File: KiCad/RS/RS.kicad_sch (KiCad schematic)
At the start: 81 parts, among them J1 TSM-104-01-L-SH, J2 Conn_01x04_Socket, J3 SPI1, J4 SPI2, J5 XY2500V-B(5.0)-2P, J6 Screw_Terminal_01x12, Q1 AO3400A, Q2 FMMT491A, SW1 SW_Push, U1 MCP1700T-3302E/TT, U2 LM2596S-5, U3 STM32C562KET6, U4 TLP185, U5 RV-3028-C7, Y1 24MHz CL=8pF ESR=50Ω

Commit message: ADD: ST87M01-1301 Modem.
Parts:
- removed J4: SPI2, Connector_IDC:IDC-Header_2x04_P2.54mm_Vertical_SMD, symbol Connector_Generic:Conn_02x04_Odd_Even
- removed R12, R4, R7: 10k, Resistor_SMD:R_0805_2012Metric_Pad1.20x1.40mm_HandSolder, symbol Device:R
- L2: value 1kΩ/100kHz -> 1kΩ/100MHz
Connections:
- net SPI2_MOSI is gone; now on net D_OUT1_M: U3.19 (PA8)
- net SPI2_NSS is gone; now on net RTC_CLK: U3.27 (PB4)
- net D_OUT1_M: no longer U3.20 (PA9)
- net D_OUT2_M: now also U3.20 (PA9); no longer U3.21 (PA11)
- net GND: no longer U3.31 (PB8-BOOT0)
- net I2C1_SCL: no longer R5.2, U3.29 (PB6)
- net SPI1_MISO: no longer R11.1, U3.12 (PA6)
- net SPI1_MOSI: no longer U3.28 (PB5)
- net SPI1_NSS: no longer R3.2, U3.25 (PA15)
- net SPI1_SCK: no longer U3.11 (PA5)
- net SPI2_IRQ renamed SWO
- net SPI2_MISO renamed MODEM_WAKE_UP
- net SPI2_SCK renamed MODEM_RX
- new net I2C_SCL: R5.2, U3.29 (PB6)
- new net MODEM_RST: U3.31 (PB8-BOOT0)
- new net MODEM_TX: U3.21 (PA11)
- new net SPI_MISO: R11.1, U3.12 (PA6)
- new net SPI_MOSI: U3.28 (PB5)
- new net SPI_NSS: R3.2, U3.25 (PA15)
- new net SPI_SCK: U3.11 (PA5)
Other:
- note removed: "SPI2"
- moved on the sheet: BT1, C13, C15, C17, C18, R10, R11, R13, R18, R3, R5, R6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

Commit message: FIX: BOM, SCH.
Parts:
- removed J1: TSM-104-01-L-SH, CodeDog:SAMTEC_TSM-104-01-L-SH, symbol Connector:Conn_01x04_Pin
- removed J2: Conn_01x04_Socket, CodeDog:SAMTEC_TSM-104-01-L-SH, symbol Connector:Conn_01x04_Socket
- removed J3: SPI1, Connector_IDC:IDC-Header_2x04_P2.54mm_Vertical_SMD, symbol Connector_Generic:Conn_02x04_Odd_Even
- removed Q2: FMMT491A, Package_TO_SOT_SMD:SOT-23, symbol CustomSymbols:FMMT491A
- added Q2: BC817, Package_TO_SOT_SMD:SOT-23, symbol Transistor_BJT:BC817
- added R12, R14, R15, R18, R6, R7, R8, R9: 0R, Resistor_SMD:R_0805_2012Metric_Pad1.20x1.40mm_HandSolder, symbol Device:R
- added TP5, TP6, TP7, TP8, TP9: Test Point, Connector_PinHeader_2.54mm:PinHeader_1x01_P2.54mm_Vertical, symbol Connector_Generic:Conn_01x01
- BT1: value DS1092-04-B6P -> 1056; footprint CodeDog:BatteryHolder_Keystone_106_1x20mm -> CodeDog:BAT_1056; symbol Device:Battery_Cell -> CodeDog:1056; MANUFACTURER (none) -> Keystone; MAXIMUM_PACKAGE_HEIGHT (none) -> 3.99mm; PARTREV (none) -> D; SNAPEDA_PN (none) -> 1056; STANDARD (none) -> Manufacturer Recommendations
- C1, C15, C3, C8: Mfg Part # UMK107BJ105KA-T -> GMC21X7R105K50NT; URL https://www.digikey.pl/en/products/detail/taiyo-yuden/UMK10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 -> https://www.digikey.pl/en/products/detail/cal-chip-electron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
- C11, C12: Mfg Part # 600F120JT250XT4K -> CML0805C0G120JT50V; URL https://www.digikey.pl/en/products/detail/kyocera-avx/600F1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 -> https://www.digikey.pl/en/products/detail/stackpole-electro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
- C13: Mfg Part # CC0805MRX7R0BB102 -> CL21B102KBANNNC; URL https://www.digikey.pl/en/products/detail/yageo/CC0805MRX7R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 -> https://www.digikey.pl/en/products/detail/samsung-electro-m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
- C16: Mfg Part # GRM21BR71A225KA01L -> 0805B225K250CT; URL https://www.digikey.pl/en/products/detail/murata-electronic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 -> https://www.digikey.pl/en/products/detail/walsin-technology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
- C18: value 220u/16V -> 10μ/10V; footprint Capacitor_SMD:C_1206_3216Metric -> Capacitor_SMD:C_1206_3216Metric_Pad1.33x1.80mm_HandSolder; Mfg Part # GRM31CR60J227ME11L -> GMC31Y5V106Z10NT; URL https://www.digikey.pl/en/products/detail/murata-electronic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 -> https://www.digikey.pl/en/products/detail/cal-chip-electron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
- C4: URL https://www.digikey.pl/en/products/detail/samsung-electro-m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 -> https://www.digikey.pl/en/products/detail/murata-electronic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
- D1: value B1701USD-20D000114U1930 -> LED red; URL (none) -> https://www.digikey.pl/en/products/detail/harvatek-corporat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
- D2: value B1701NG--20D000314U1930 -> LED red; Mfg Part # B1701NG--20D000314U1930 -> B1701USD-20D000114U1930; URL (none) -> https://www.digikey.pl/en/products/detail/harvatek-corporat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
- D3: symbol PCM_Diode_Schottky_AKL:SS34 -> Device:D_Schottky_Filled; URL (none) -> https://www.digikey.pl/en/products/detail/goodwork/SS56/292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
- D4: value BZV55C3V3-LGE -> 3V3; footprint Diode_SMD:D_MiniMELF -> Diode_SMD:D_SOD-523; Mfg Part # BZV55C3V3 -> BZX584B3V3; URL (none) -> https://www.digikey.pl/en/products/detail/shenzhen-slkormic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
- D5: footprint Diode_SMD:D_SOD-923 -> Diode_SMD:D_SOD-123; Mfg Part # CDZVT2R3.6B -> BZT52C3V6; URL https://www.digikey.pl/en/products/detail/rohm-semiconducto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 -> https://www.digikey.pl/en/products/detail/smc-diode-solutio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
- D6: value B1701UY--20D000214U1930 -> LED amber; URL (none) -> https://www.digikey.pl/en/products/detail/harvatek-corporat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
- J1: renamed from J5; now not fitted
- J2: renamed from J6; now not fitted
- Q1: Mfg Part # (none) -> AO3400A; URL (none) -> https://www.digikey.pl/en/products/detail/umw/AO3400A/16705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
- renumbered R8 to R10, R9 to R11, R10 to R13, R11 to R16, R13 to R17, R14 to R19, R15 to R20, R17 to R21, R19 to R22, R18 to R23, R16 to R24, R20 to R25, R21 to R26, R22 to R27, R23 to R28, R24 to R29, R25 to R30, R26 to R31, R5 to R4, R6 to R5, TP5 to TP10, TP6 to TP11, TP7 to TP12, TP8 to TP13, TP9 to TP14, TP10 to TP15, TP11 to TP16, TP12 to TP17, TP13 to TP18
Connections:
- net I2C1_SCL is gone; now on net I2C_SCL: U5.3 (SCL)
- net GND: now also BT1.N, C18.1, U3.32 (VSS), Q2.2 (E); no longer BT1.2 (-), C18.2
- net MODEM_RST: now also R7.1; no longer U3.31 (PB8-BOOT0)
- net MODEM_RX: now also R12.2; no longer U3.22 (PA12)
- net MODEM_TX: now also R14.2; no longer U3.21 (PA11)
- net MODEM_WAKE_UP: now also R15.2; no longer U3.13 (PA7)
- net at R29.2, R31.1: now also Q2.1 (B)
- net at R25.2, R26.1: now also Q2.3 (C)
- net NRST: now reaches C14.2, R10.2, SW1.2, U3.4 (NRST)
- net A_- renamed RCS
- net SPI1_IRQ renamed SPI_IRQ
- new net: R6.1, R7.2, U3.31 (PB8-BOOT0)
- new net: BT1.P, C18.2, U5.6 (VBACKUP)
- new net: R15.1, R18.2, U3.13 (PA7)
- new net: R14.1, R9.1, U3.21 (PA11)
- new net: R12.1, R8.1, U3.22 (PA12)
- new net VANT: TP9.1 (Pin_1)
- new net VEXT: TP7.1 (Pin_1)
- new net VMOD: TP6.1 (Pin_1)
- new net VMOD_PG: TP5.1 (Pin_1)
- new net VSIM: TP8.1 (Pin_1)
- new net X_MODEM_RST: R6.2
- new net X_MODEM_RX: R8.2
- new net X_MODEM_TX: R9.2
- new net X_MODEM_WAKE_UP: R18.1
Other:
- note removed: "I2C1"
- note removed: "R"
- note removed: "SPI1"
- note removed: "ST-LINK"
- note removed: "Y"
- title: Remote Sensor Module MCU Sheet -> Remote Sensor Module: PSU, MCU, Analog
- moved on the sheet: BT1, C13, C15, D4, D5, D6, Q1, R11, R13, R16, R17, R19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

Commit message: ADD: RF connections.
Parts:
- L2: footprint (none) -> Inductor_SMD:L_0805_2012Metric_Pad1.05x1.20mm_HandSolder
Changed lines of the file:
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@@
 			)
 		)
-		(property "Footprint" ""
+		(property "Footprint" "Inductor_SMD:L_0805_2012Metric_Pad1.05x1.20mm_HandSolder"
 			(at 27.94 60.96 0)
 			(hide yes)

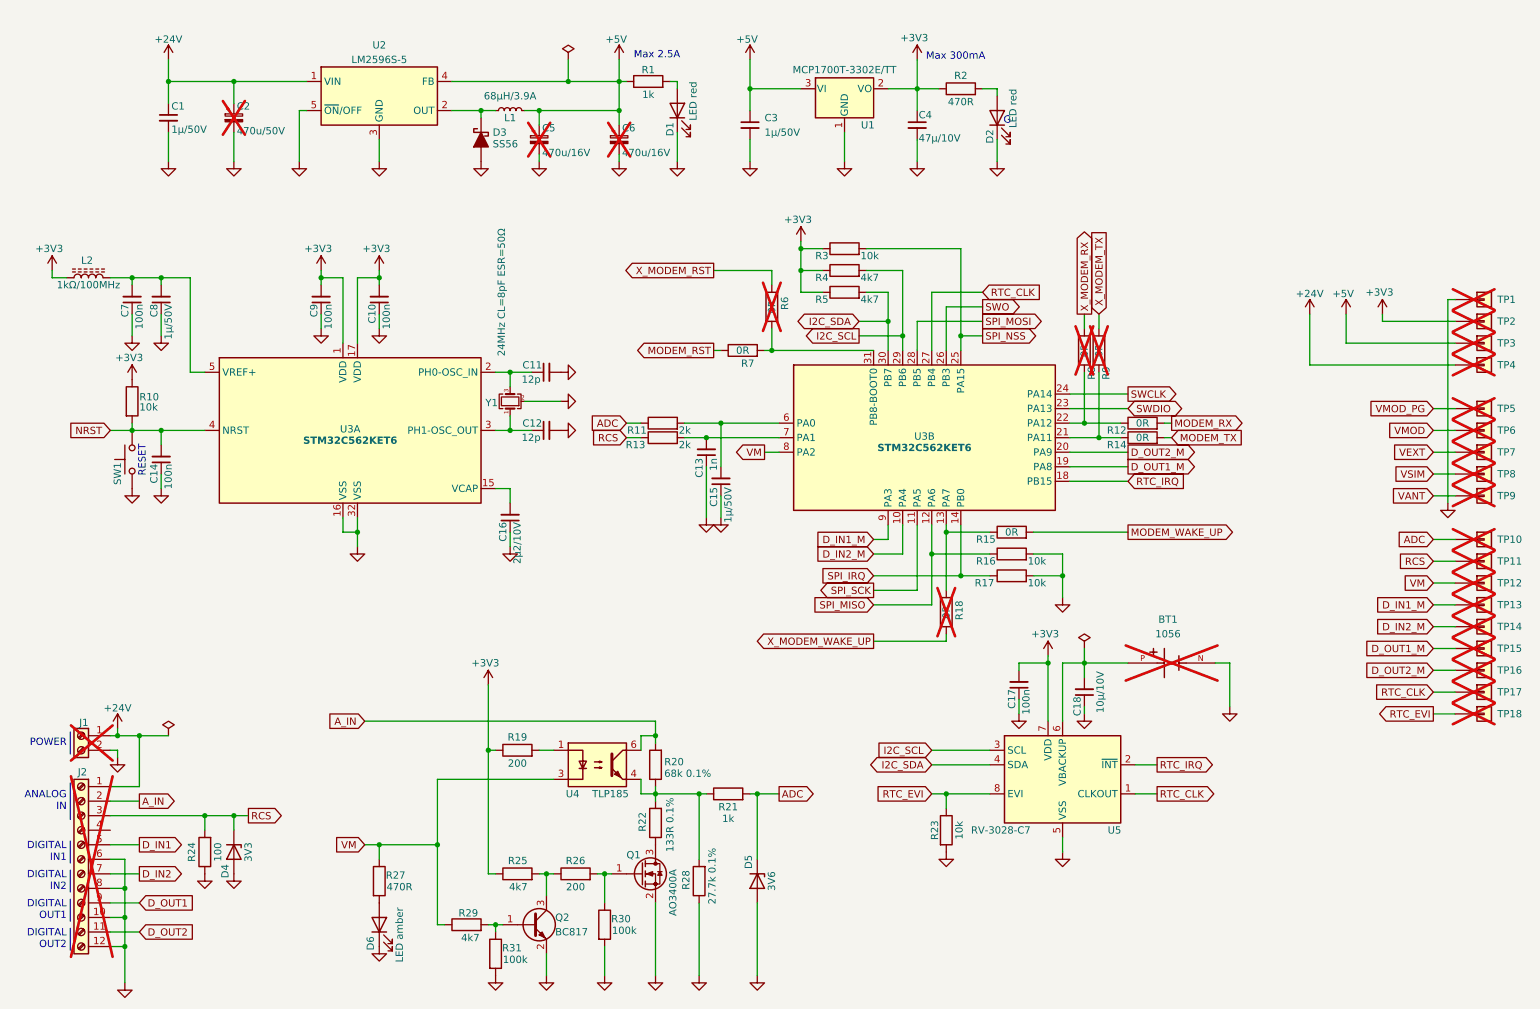
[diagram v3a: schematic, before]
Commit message: FIX: 0805 to 0402, modem leds+drivers
ADD: Modem part completed!
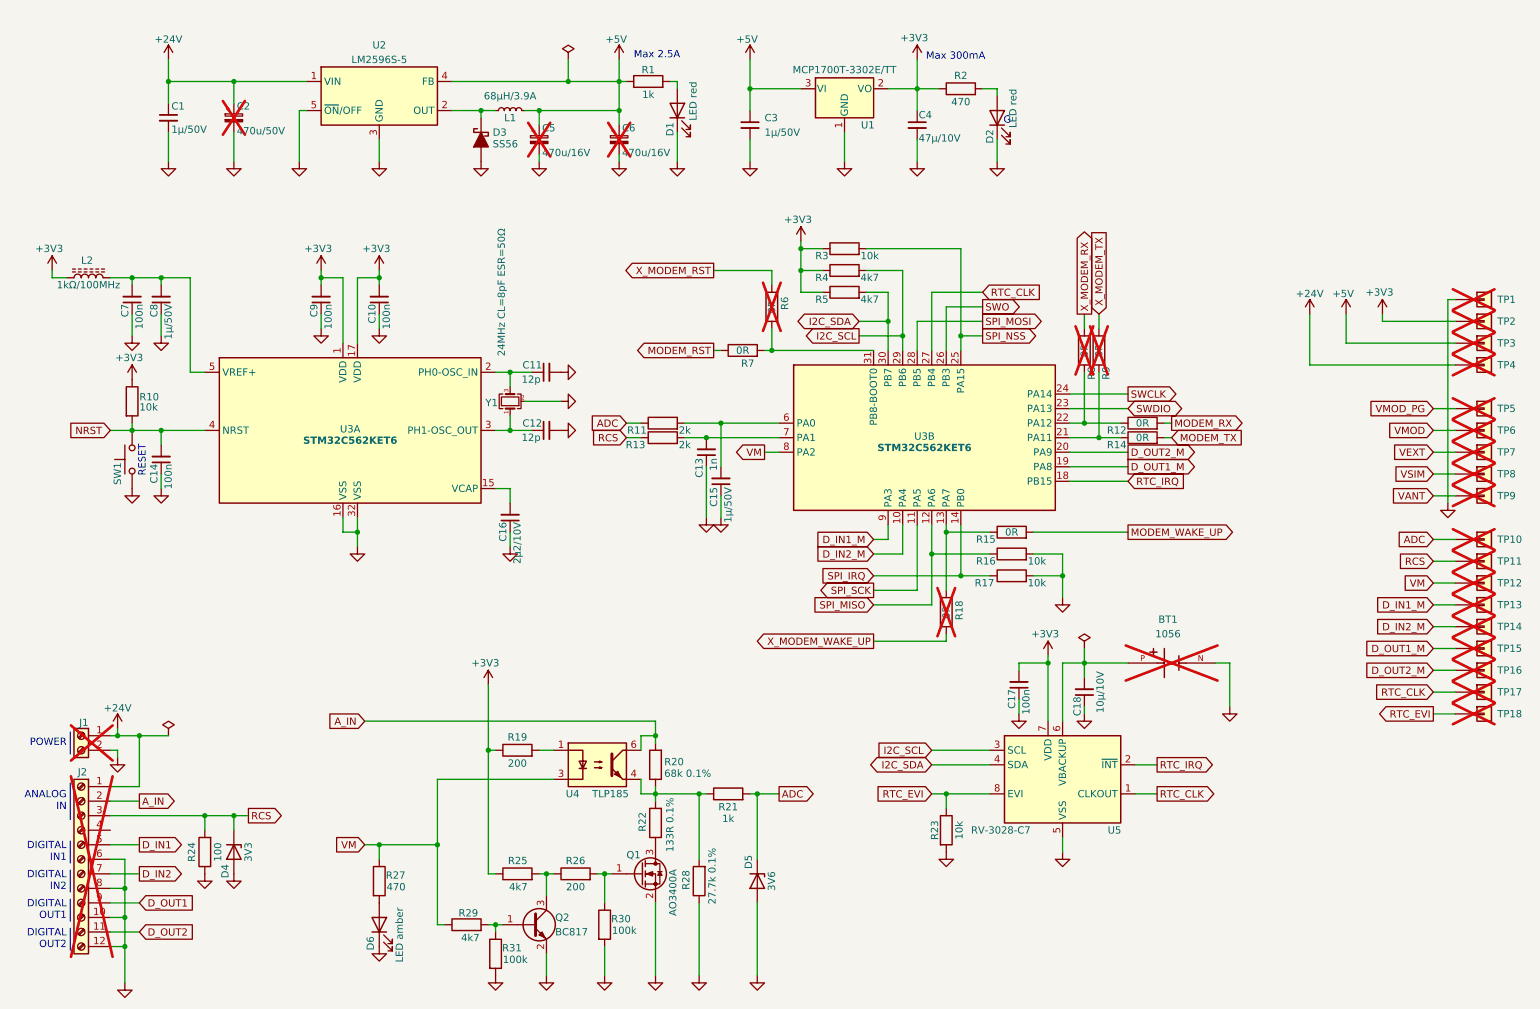
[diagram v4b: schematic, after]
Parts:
- R10, R16, R17, R23, R3: footprint Resistor_SMD:R_0805_2012Metric_Pad1.20x1.40mm_HandSolder -> Resistor_SMD:R_0402_1005Metric_Pad0.72x0.64mm_HandSolder; Mfg Part # CR0805JB10KS01 -> RMCF0402FT10K0; URL https://www.digikey.pl/en/products/detail/nextgen-component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 -> https://www.digikey.pl/en/products/detail/stackpole-electro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
- R2, R27: value 470R -> 470
- R25, R29, R4, R5: footprint Resistor_SMD:R_0805_2012Metric_Pad1.20x1.40mm_HandSolder -> Resistor_SMD:R_0402_1005Metric_Pad0.72x0.64mm_HandSolder; Mfg Part # CR0805JB4K7S01 -> RC0402FR-074K7L; URL https://www.digikey.pl/en/products/detail/nextgen-component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 -> https://www.digikey.pl/en/products/detail/yageo/RC0402FR-07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
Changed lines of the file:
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@@
 			)
 		)
-		(property "Footprint" "Resistor_SMD:R_0805_2012Metric_Pad1.20x1.40mm_HandSolder"
+		(property "Footprint" "Resistor_SMD:R_0402_1005Metric_Pad0.72x0.64mm_HandSolder"
 			(at 160.02 57.658 90)
 			(hide yes)
@@
 			)
 		)
-		(property "Datasheet" ""
+		(property "Datasheet" "https://www.seielect.com/catalog/SEI-RMCF_RMCP.pdf"
 			(at 160.02 55.88 0)
 			(hide yes)
@@
 			)
 		)
-		(property "Mfg Part #" "CR0805JB10KS01"
+		(property "Mfg Part #" "RMCF0402FT10K0"
 			(at 160.02 55.88 0)
 			(hide yes)
@@
 			)
 		)
-		(property "URL" "https://www.digikey.pl/en/products/detail/nextgen-components/CR0805JB10KS01/18157959"
+		(property "URL" "https://www.digikey.pl/en/products/detail/stackpole-electronics-inc/RMCF0402FT10K0/1761433"
 			(at 160.02 55.88 90)
 			(hide yes)
@@
 			)
 		)
-		(property "Footprint" "Resistor_SMD:R_0805_2012Metric_Pad1.20x1.40mm_HandSolder"
+		(property "Footprint" "Resistor_SMD:R_0402_1005Metric_Pad0.72x0.64mm_HandSolder"
 			(at 189.23 110.998 90)
 			(hide yes)
@@
 			)
 		)
-		(property "Datasheet" ""
+		(property "Datasheet" "https://www.seielect.com/catalog/SEI-RMCF_RMCP.pdf"
 			(at 189.23 109.22 0)
 			(hide yes)
@@
 			)
 		)
-		(property "Mfg Part #" "CR0805JB10KS01"
+		(property "Mfg Part #" "RMCF0402FT10K0"
 			(at 189.23 109.22 0)
 			(hide yes)
@@
 			)
 		)
-		(property "URL" "https://www.digikey.pl/en/products/detail/nextgen-components/CR0805JB10KS01/18157959"
+		(property "URL" "https://www.digikey.pl/en/products/detail/stackpole-electronics-inc/RMCF0402FT10K0/1761433"
 			(at 189.23 109.22 90)
 			(hide yes)
@@
 			)
 		)
-		(property "Footprint" "Resistor_SMD:R_0805_2012Metric_Pad1.20x1.40mm_HandSolder"
+		(property "Footprint" "Resistor_SMD:R_0402_1005Metric_Pad0.72x0.64mm_HandSolder"
 			(at 160.02 65.278 90)
 			(hide yes)
@@
 			)
 		)
-		(property "Datasheet" ""
+		(property "Datasheet" "https://yageogroup.com/content/datasheet/asset/file/PYU-RC_GROUP_51_ROHS_L"
 			(at 160.02 63.5 0)
 			(hide yes)
@@
 			)
 		)
-		(property "Mfg Part #" "CR0805JB4K7S01"
+		(property "Mfg Part #" "RC0402FR-074K7L"
 			(at 160.02 63.5 0)
 			(hide yes)
@@
 			)
 		)
-		(property "URL" "https://www.digikey.pl/en/products/detail/nextgen-components/CR0805JB4K7S01/15761328"
+		(property "URL" "https://www.digikey.pl/en/products/detail/yageo/RC0402FR-074K7L/2827563"
 			(at 160.02 63.5 0)
 			(hide yes)
@@
 			)
 		)
-		(property "Footprint" "Resistor_SMD:R_0805_2012Metric_Pad1.20x1.40mm_HandSolder"
+		(property "Footprint" "Resistor_SMD:R_0402_1005Metric_Pad0.72x0.64mm_HandSolder"
 			(at 160.02 61.468 90)
 			(hide yes)
@@
 			)
 		)
-		(property "Datasheet" ""
+		(property "Datasheet" "https://yageogroup.com/content/datasheet/asset/file/PYU-RC_GROUP_51_ROHS_L"
 			(at 160.02 59.69 0)
 			(hide yes)
@@
 			)
 		)
-		(property "Mfg Part #" "CR0805JB4K7S01"
+		(property "Mfg Part #" "RC0402FR-074K7L"
 			(at 160.02 59.69 0)
 			(hide yes)
@@
 			)
 		)
-		(property "URL" "https://www.digikey.pl/en/products/detail/nextgen-components/CR0805JB4K7S01/15761328"
+		(property "URL" "https://www.digikey.pl/en/products/detail/yageo/RC0402FR-074K7L/2827563"
 			(at 160.02 59.69 0)
 			(hide yes)
@@
 			)
 		)
-		(property "Footprint" "Resistor_SMD:R_0805_2012Metric_Pad1.20x1.40mm_HandSolder"
+		(property "Footprint" "Resistor_SMD:R_0402_1005Metric_Pad0.72x0.64mm_HandSolder"
 			(at 102.87 166.878 90)
 			(hide yes)
@@
 			)
 		)
-		(property "Datasheet" ""
+		(property "Datasheet" "https://yageogroup.com/content/datasheet/asset/file/PYU-RC_GROUP_51_ROHS_L"
 			(at 102.87 165.1 0)
 			(hide yes)
@@
 			)
 		)
-		(property "Mfg Part #" "CR0805JB4K7S01"
+		(property "Mfg Part #" "RC0402FR-074K7L"
 			(at 102.87 165.1 0)
 			(hide yes)
@@
 			)
 		)
-		(property "URL" "https://www.digikey.pl/en/products/detail/nextgen-components/CR0805JB4K7S01/15761328"
+		(property "URL" "https://www.digikey.pl/en/products/detail/yageo/RC0402FR-074K7L/2827563"
 			(at 102.87 165.1 90)
 			(hide yes)
@@
 			)
 		)
-		(property "Footprint" "Resistor_SMD:R_0805_2012Metric_Pad1.20x1.40mm_HandSolder"
+		(property "Footprint" "Resistor_SMD:R_0402_1005Metric_Pad0.72x0.64mm_HandSolder"
 			(at 176.022 157.48 90)
 			(hide yes)
@@
 			)
 		)
-		(property "Datasheet" ""
+		(property "Datasheet" "https://www.seielect.com/catalog/SEI-RMCF_RMCP.pdf"
 			(at 177.8 157.48 0)
 			(hide yes)
@@
 			)
 		)
-		(property "Mfg Part #" "CR0805JB10KS01"
+		(property "Mfg Part #" "RMCF0402FT10K0"
 			(at 177.8 157.48 0)
 			(hide yes)
@@
 			)
 		)
-		(property "URL" "https://www.digikey.pl/en/products/detail/nextgen-components/CR0805JB10KS01/18157959"
+		(property "URL" "https://www.digikey.pl/en/products/detail/stackpole-electronics-inc/RMCF0402FT10K0/1761433"
 			(at 177.8 157.48 90)
 			(hide yes)
@@
 			)
 		)
-		(property "Value" "470R"
+		(property "Value" "470"
 			(at 80.01 167.386 0)
 			(show_name no)
@@
 			)
 		)
-		(property "Footprint" "Resistor_SMD:R_0805_2012Metric_Pad1.20x1.40mm_HandSolder"
+		(property "Footprint" "Resistor_SMD:R_0402_1005Metric_Pad0.72x0.64mm_HandSolder"
 			(at 33.782 82.55 90)
 			(hide yes)
@@
 			)
 		)
-		(property "Datasheet" ""
+		(property "Datasheet" "https://www.seielect.com/catalog/SEI-RMCF_RMCP.pdf"
 			(at 35.56 82.55 0)
 			(hide yes)
@@
 			)
 		)
-		(property "Mfg Part #" "CR0805JB10KS01"
+		(property "Mfg Part #" "RMCF0402FT10K0"
 			(at 35.56 82.55 0)
 			(hide yes)
@@
 			)
 		)
-		(property "URL" "https://www.digikey.pl/en/products/detail/nextgen-components/CR0805JB10KS01/18157959"
+		(property "URL" "https://www.digikey.pl/en/products/detail/stackpole-electronics-inc/RMCF0402FT10K0/1761433"
 			(at 35.56 82.55 0)
 			(hide yes)
@@
 			)
 		)
-		(property "Footprint" "Resistor_SMD:R_0805_2012Metric_Pad1.20x1.40mm_HandSolder"
+		(property "Footprint" "Resistor_SMD:R_0402_1005Metric_Pad0.72x0.64mm_HandSolder"
 			(at 189.23 114.808 90)
 			(hide yes)
@@
 			)
 		)
-		(property "Datasheet" ""
+		(property "Datasheet" "https://www.seielect.com/catalog/SEI-RMCF_RMCP.pdf"
 			(at 189.23 113.03 0)
 			(hide yes)
@@
 			)
 		)
-		(property "Mfg Part #" "CR0805JB10KS01"
+		(property "Mfg Part #" "RMCF0402FT10K0"
 			(at 189.23 113.03 0)
 			(hide yes)
@@
 			)
 		)
-		(property "URL" "https://www.digikey.pl/en/products/detail/nextgen-components/CR0805JB10KS01/18157959"
+		(property "URL" "https://www.digikey.pl/en/products/detail/stackpole-electronics-inc/RMCF0402FT10K0/1761433"
 			(at 189.23 113.03 90)
 			(hide yes)
@@
 			)
 		)
-		(property "Value" "470R"
+		(property "Value" "470"
 			(at 180.34 30.226 90)
 			(show_name no)
@@
 			)
 		)
-		(property "Footprint" "Resistor_SMD:R_0805_2012Metric_Pad1.20x1.40mm_HandSolder"
+		(property "Footprint" "Resistor_SMD:R_0402_1005Metric_Pad0.72x0.64mm_HandSolder"
 			(at 93.98 175.768 90)
 			(hide yes)
@@
 			)
 		)
-		(property "Datasheet" ""
+		(property "Datasheet" "https://yageogroup.com/content/datasheet/asset/file/PYU-RC_GROUP_51_ROHS_L"
 			(at 93.98 173.99 0)
 			(hide yes)
@@
 			)
 		)
-		(property "Mfg Part #" "CR0805JB4K7S01"
+		(property "Mfg Part #" "RC0402FR-074K7L"
 			(at 93.98 173.99 0)
 			(hide yes)
@@
 			)
 		)
-		(property "URL" "https://www.digikey.pl/en/products/detail/nextgen-components/CR0805JB4K7S01/15761328"
+		(property "URL" "https://www.digikey.pl/en/products/detail/yageo/RC0402FR-074K7L/2827563"
 			(at 93.98 173.99 90)
 			(hide yes)
